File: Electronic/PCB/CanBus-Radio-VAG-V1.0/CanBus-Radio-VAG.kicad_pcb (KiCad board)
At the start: 2 copper layers, 39.9 x 45 mm, 35 parts, among them J1 UART, J2 ICSP, J3 CAR, SW1 SW_Push-Switch, U1 MCP2515-xSO, U2 TJA1050T, U3 ATmega328P-PU, U4 MP2307, Y1 8MHz, Y2 16MHz

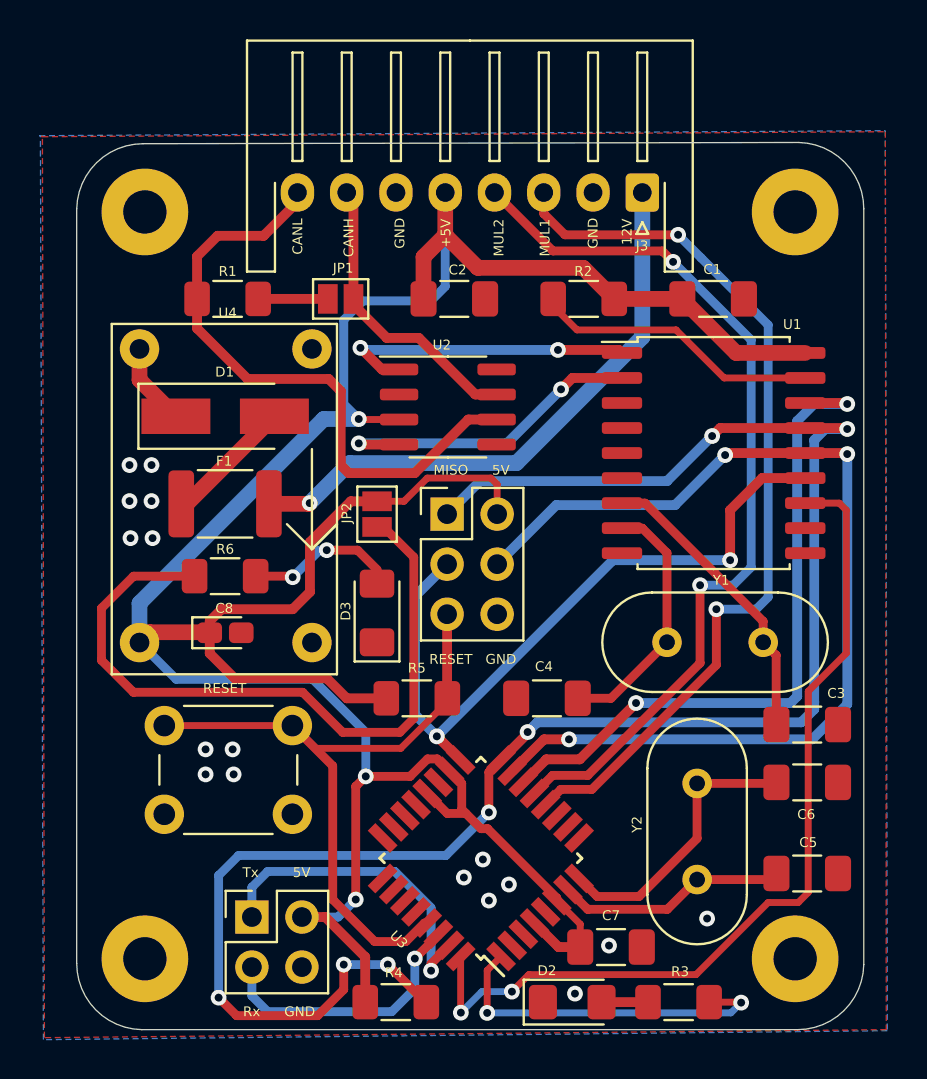
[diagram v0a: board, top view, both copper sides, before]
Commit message: Added some tools and the panelize design.
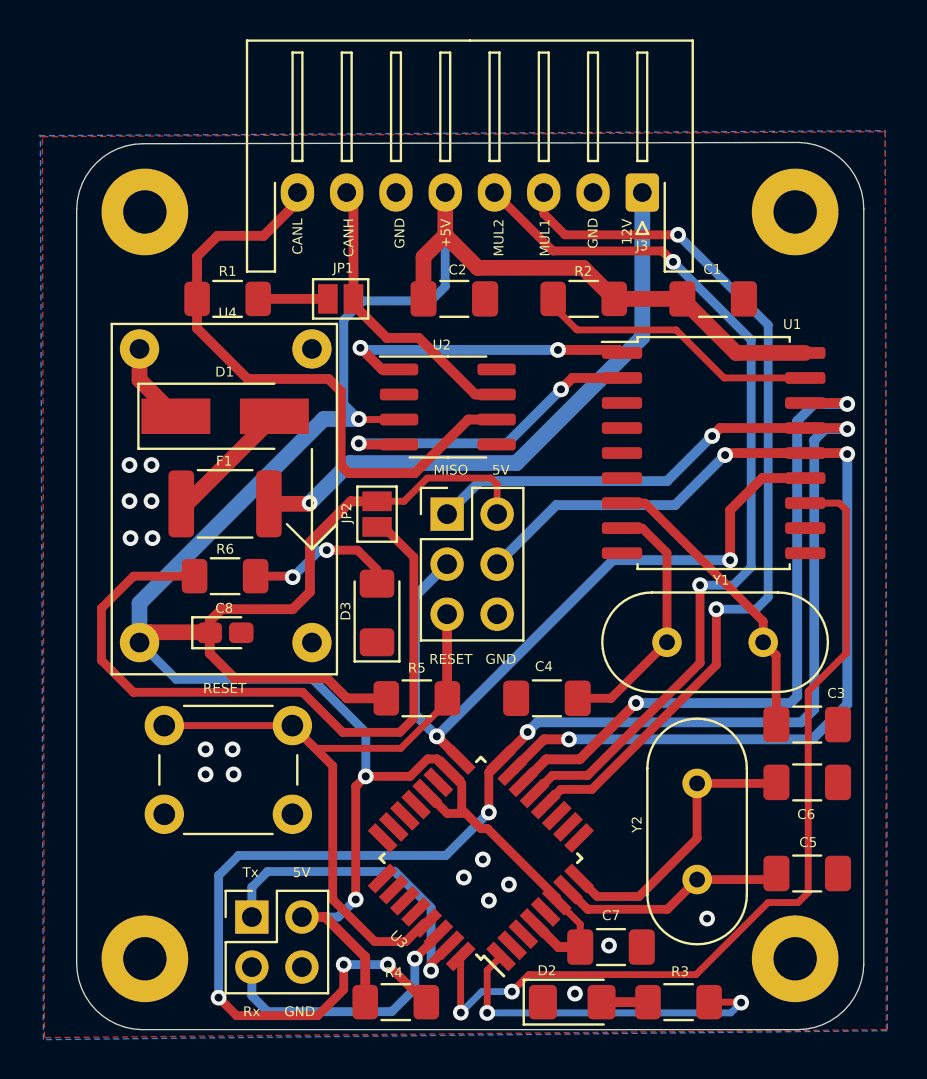
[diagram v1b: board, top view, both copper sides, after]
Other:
- net class Default removed
- net class Supply removed
